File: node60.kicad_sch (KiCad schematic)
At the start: 0 parts

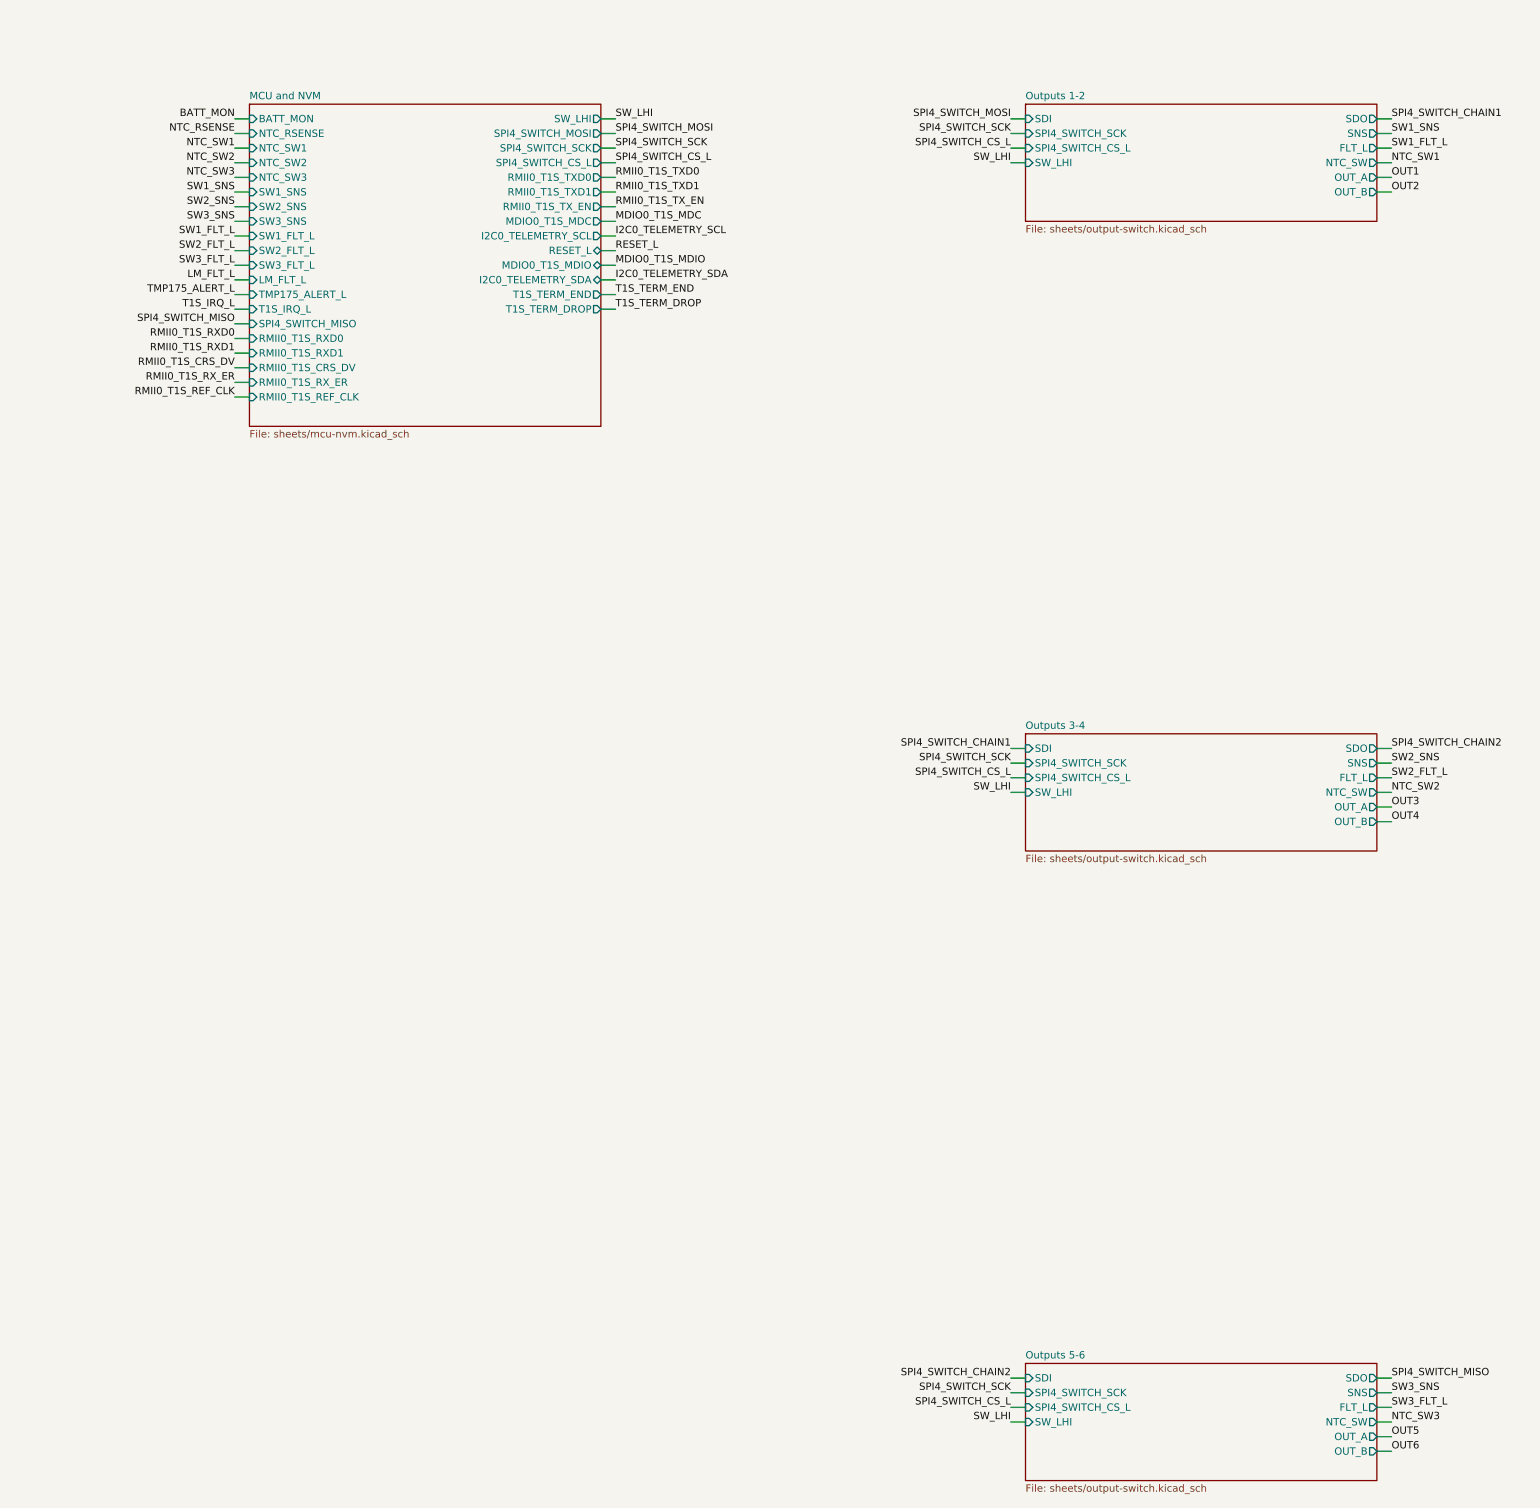
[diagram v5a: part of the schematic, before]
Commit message: One LPSPI bus per output switch (DEC-018); Zephyr as core RTOS (DEC-019)
- Split the TPS2HCS08A daisy chain into three buses: U601 on LPSPI4 (Rev A
  balls), U701 on LPSPI5 (A16/A15/B13/G16), U801 on LPSPI3 (E14/F14/E15/G15).
  The output-switch sheet now exposes generic SDI/SDO/SCK/CS_L ports.
- Per-switch SPI watchdog (400 ms) with limp-home off: a lost bus turns only
  that switch's two outputs off.
- DEC-019 records Zephyr with a driver map; pin plan reviewed against
  upstream Zephyr (EIRQ map, ADC group-channel, native PCS). No other pin moves.
- GATE-MCU-01 reopened for the eight new balls (IBIS/BSDL machine check done,
  user sign-off pending). Rev B (in progress) listed on the revisions page.

Co-Authored-By: Claude Opus 5.5 <noreply@anthropic.com>
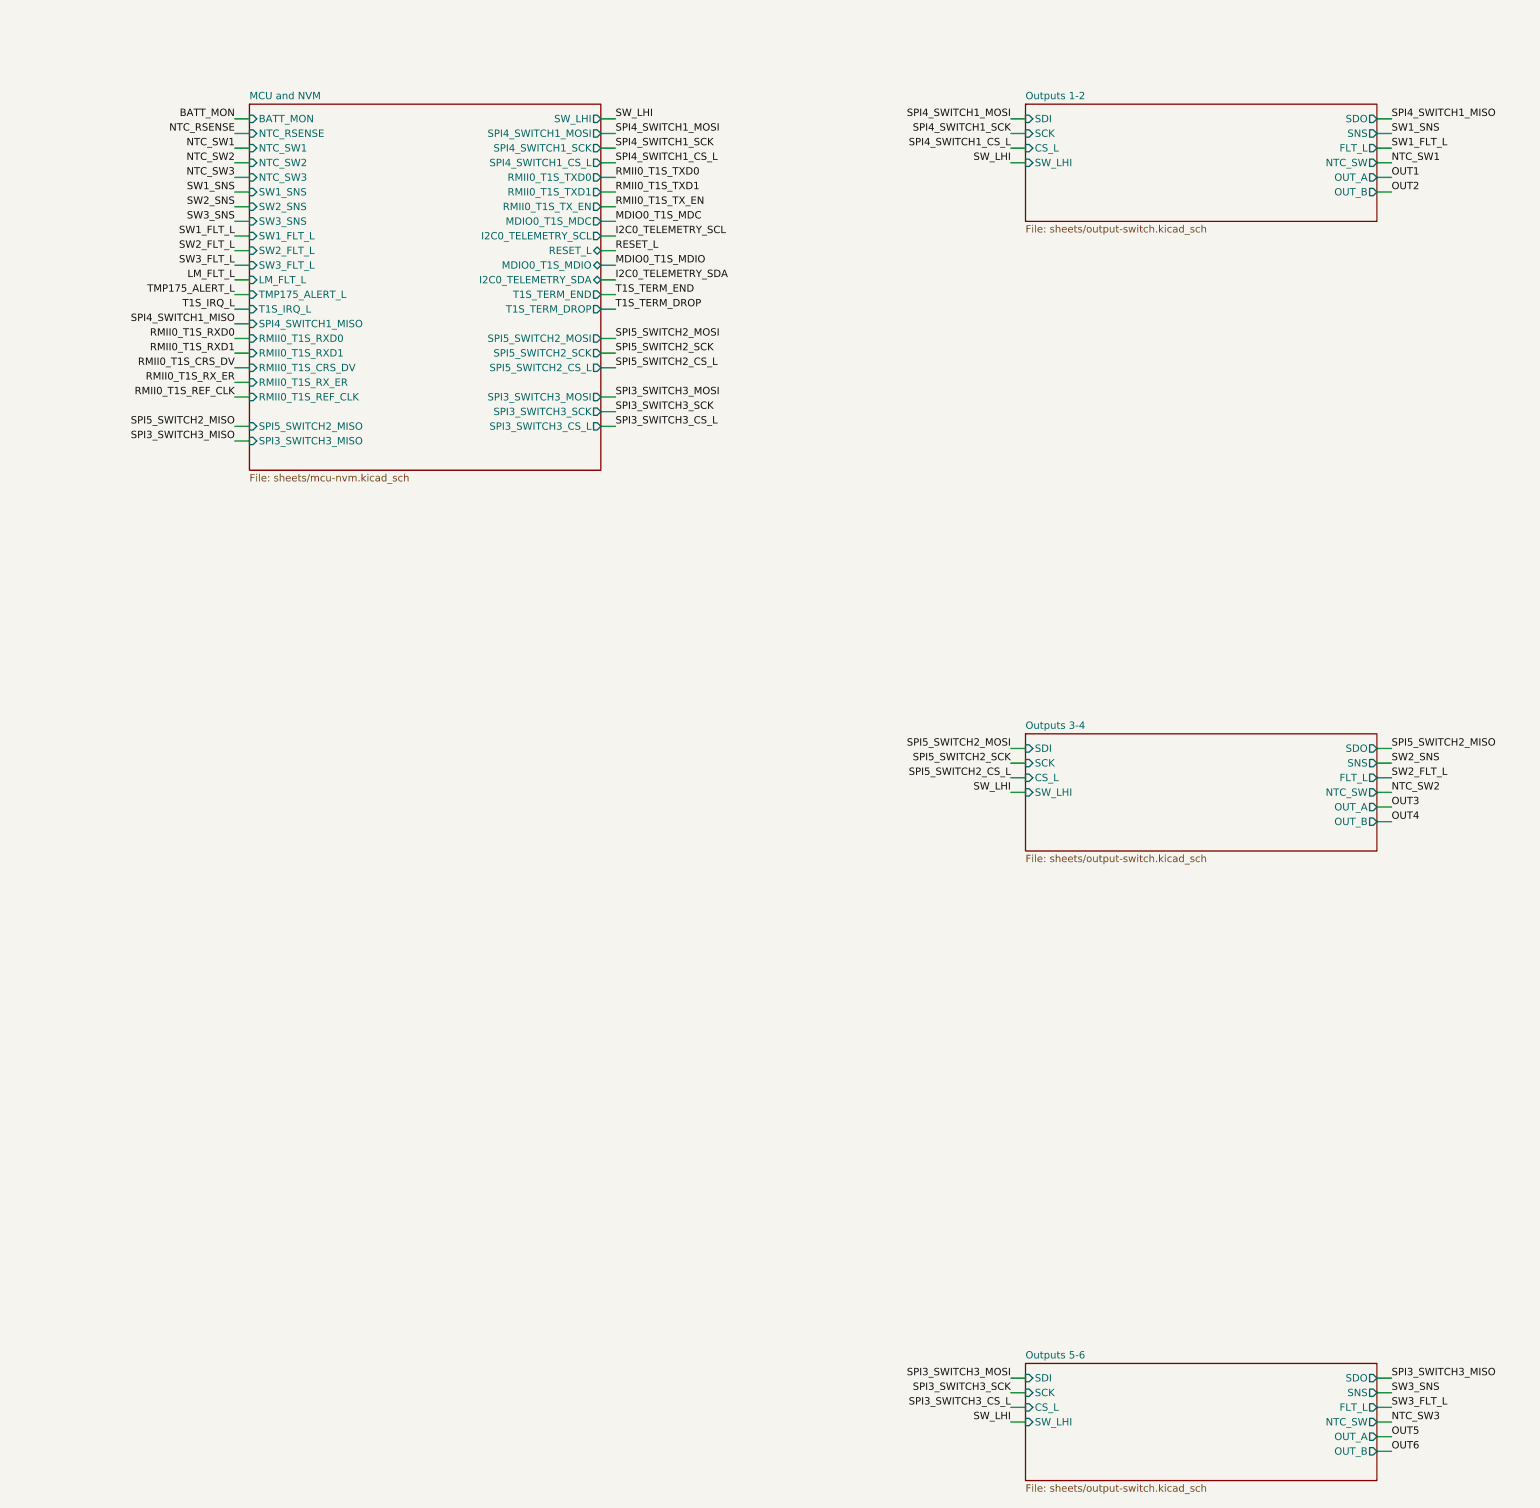
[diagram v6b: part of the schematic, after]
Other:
- sheet MCU and NVM ports: added SPI3_SWITCH3_CS_L, SPI3_SWITCH3_MISO, SPI3_SWITCH3_MOSI, SPI3_SWITCH3_SCK, SPI4_SWITCH1_CS_L, SPI4_SWITCH1_MISO, SPI4_SWITCH1_MOSI, SPI4_SWITCH1_SCK, SPI5_SWITCH2_CS_L, SPI5_SWITCH2_MISO, SPI5_SWITCH2_MOSI, SPI5_SWITCH2_SCK; removed SPI4_SWITCH_CS_L, SPI4_SWITCH_MISO, SPI4_SWITCH_MOSI, SPI4_SWITCH_SCK
- sheet Outputs 1-2 ports: added CS_L, SCK; removed SPI4_SWITCH_CS_L, SPI4_SWITCH_SCK
- sheet Outputs 3-4 ports: added CS_L, SCK; removed SPI4_SWITCH_CS_L, SPI4_SWITCH_SCK
- sheet Outputs 5-6 ports: added CS_L, SCK; removed SPI4_SWITCH_CS_L, SPI4_SWITCH_SCK
